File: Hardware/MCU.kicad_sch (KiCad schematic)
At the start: 30 parts, among them IC1 SN74AHC1G32DBVR, J3 SWD, SW1 RST, SW2 BOOT, U5 STM32L431CBTx, Y1 8M

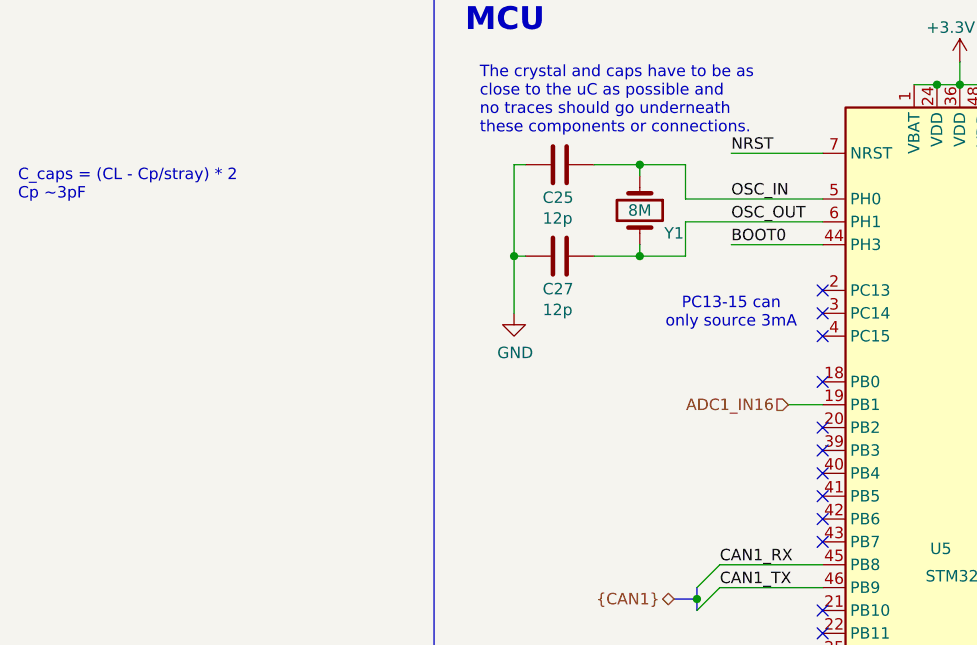
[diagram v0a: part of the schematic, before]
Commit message: differential amp for LPF
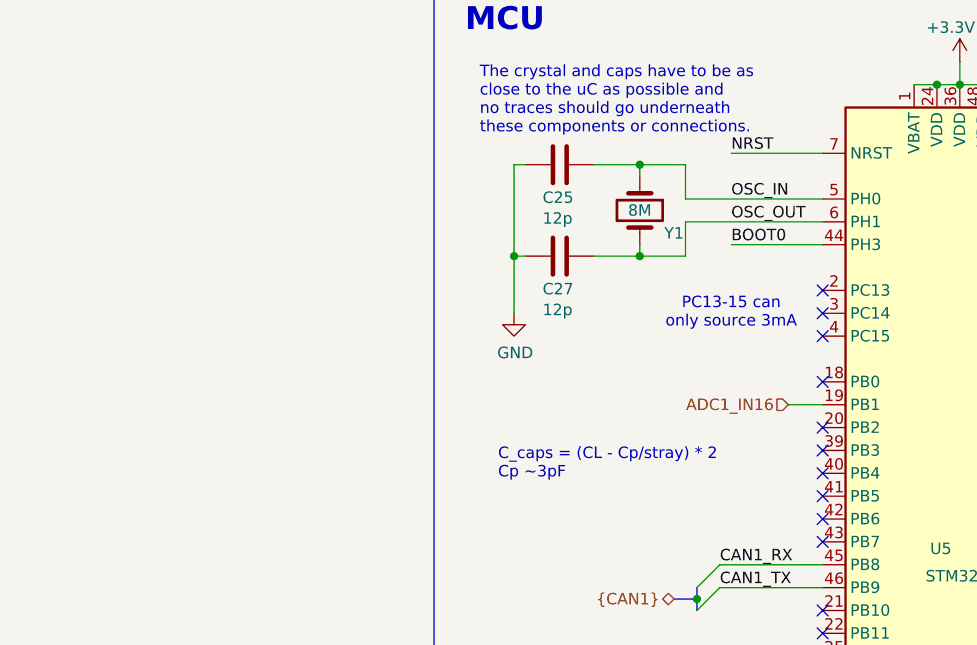
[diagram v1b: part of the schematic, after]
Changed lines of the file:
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@@
 	(text "C_caps = (CL - Cp/stray) * 2\nCp ~3pF"
 		(exclude_from_sim no)
-		(at -30.988 39.116 0)
+		(at 22.352 70.104 0)
 		(effects
 			(font

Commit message: diff amp / LPF
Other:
- note added: "Boot_GPIO is tied to PA7"
- note removed: "TODO: tie Boot_GPIO to a pin"
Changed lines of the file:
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@@
 		)
 	)
-	(text "TODO: tie Boot_GPIO to a pin"
+	(text "Boot_GPIO is tied to PA7"
 		(exclude_from_sim no)
 		(at 152.654 147.32 0)

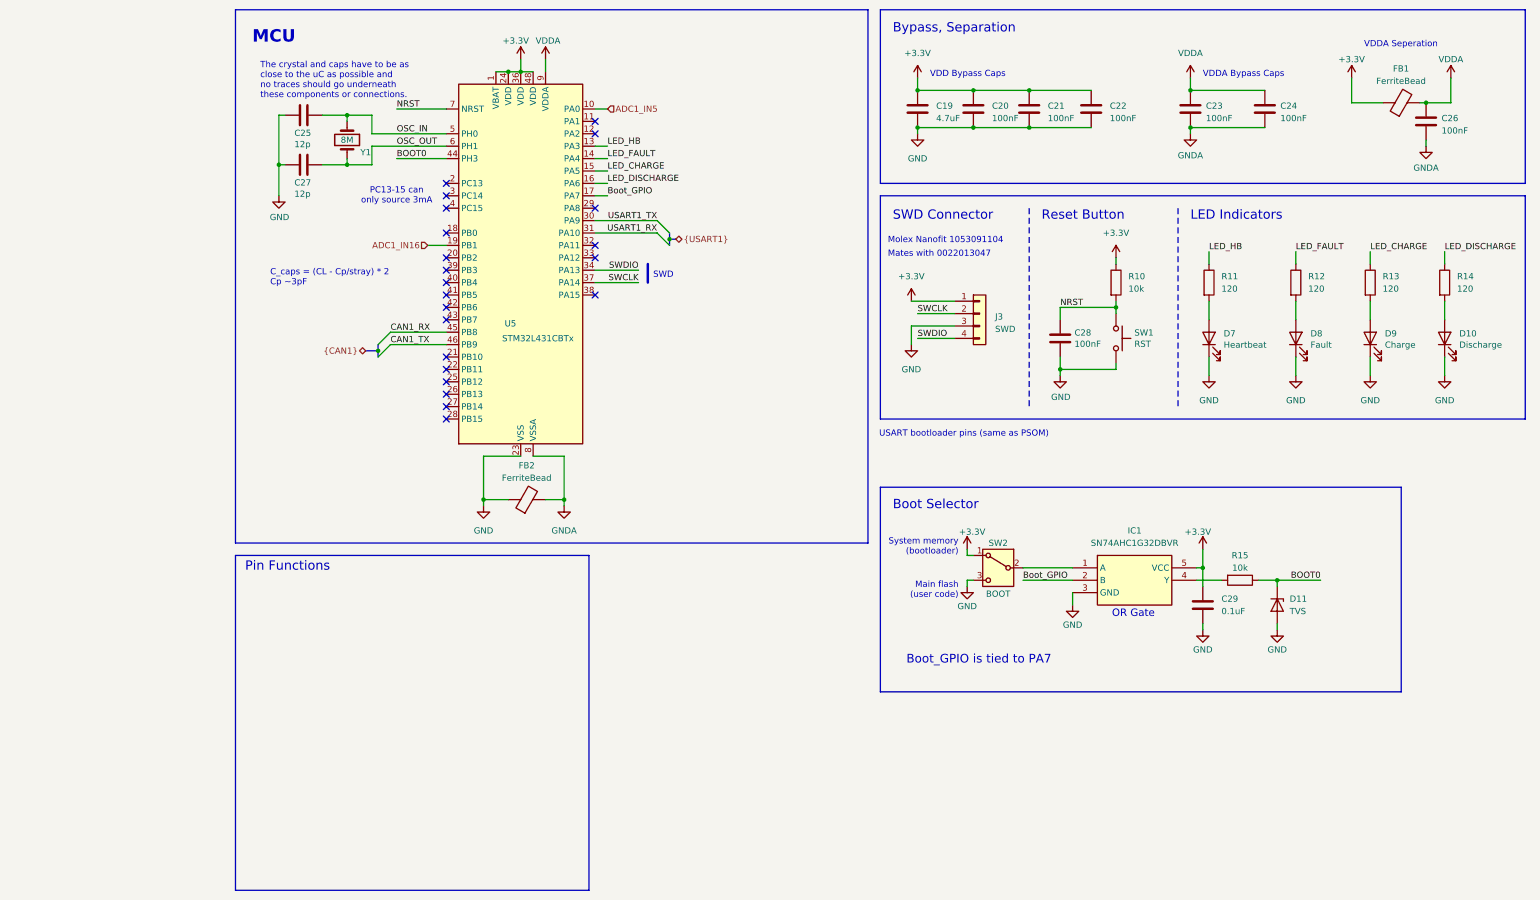
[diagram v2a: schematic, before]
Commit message: refactored and added LPF docs; added fuse, boot_gpio from USB-UART chip
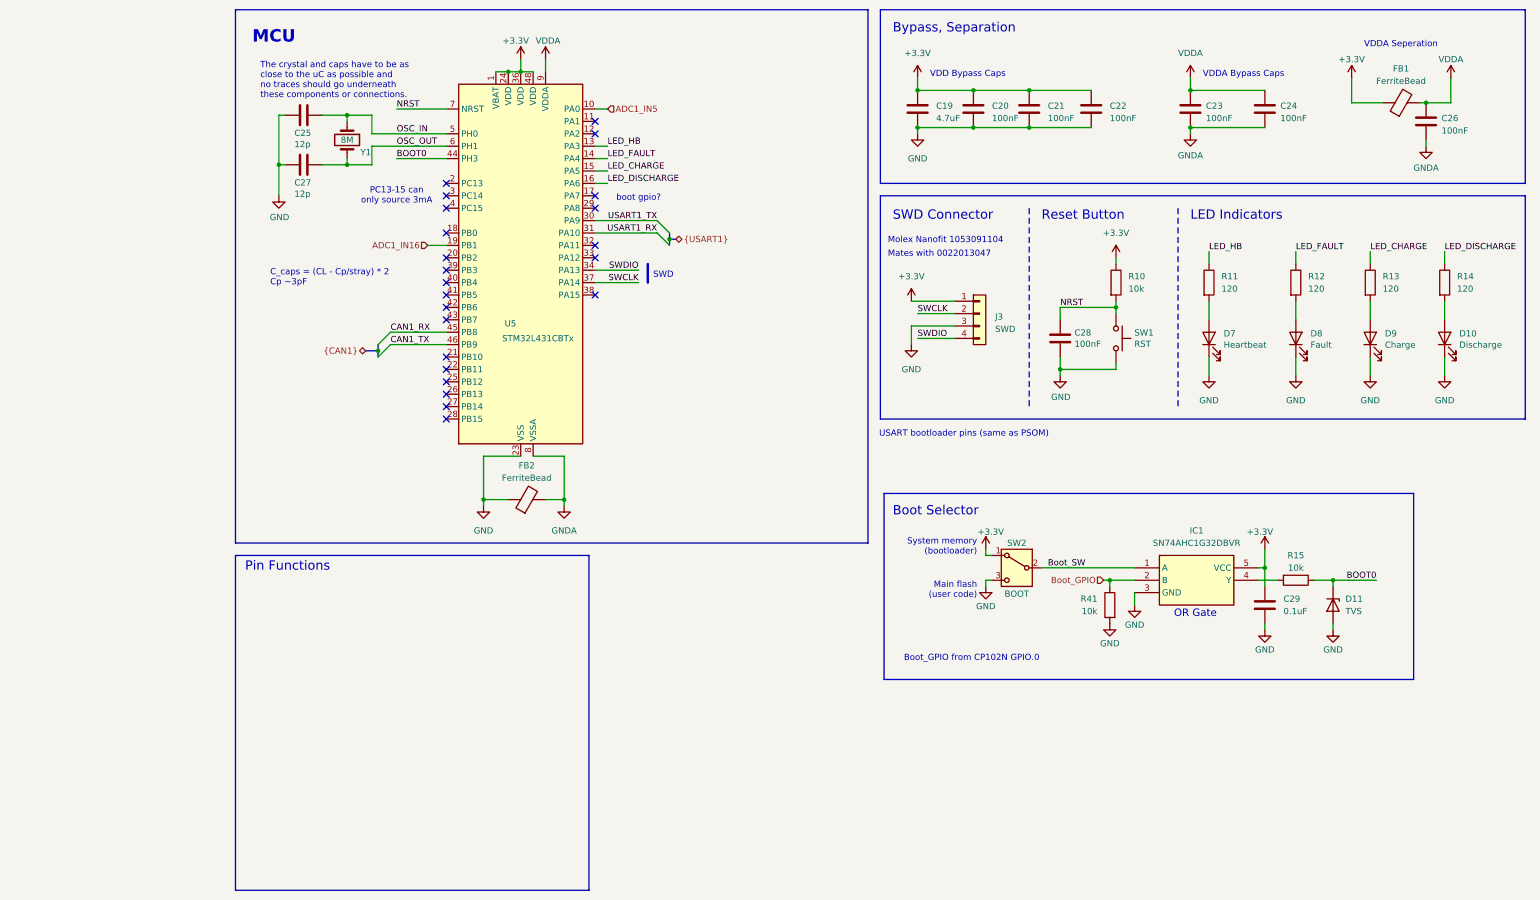
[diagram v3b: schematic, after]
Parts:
- added R41: 10k, symbol Device:R
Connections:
- net Boot_GPIO: now also R41.1; no longer U5.17 (PA7)
- net GND: now also R41.2
- net Boot_SW: now reaches IC1.1 (A), SW2.2 (B)
- no-connect marks 22 -> 23
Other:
- note added: "Boot_GPIO from CP102N GPIO.0"
- note added: "boot gpio?"
- note removed: "Boot_GPIO is tied to PA7"
- moved on the sheet: C29, D11, IC1, R15, SW2

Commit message: slightly cooked
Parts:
- R41: footprint (none) -> Resistor_SMD:R_0603_1608Metric_Pad0.98x0.95mm_HandSolder
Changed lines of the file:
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@@
 			)
 		)
-		(property "Footprint" ""
+		(property "Footprint" "Resistor_SMD:R_0603_1608Metric_Pad0.98x0.95mm_HandSolder"
 			(at 196.088 137.16 90)
 			(effects

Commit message: started layout not really but kind of
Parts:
- removed R41: 10k, Resistor_SMD:R_0603_1608Metric_Pad0.98x0.95mm_HandSolder, symbol Device:R
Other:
- moved on the sheet: C29, D11, IC1, R15

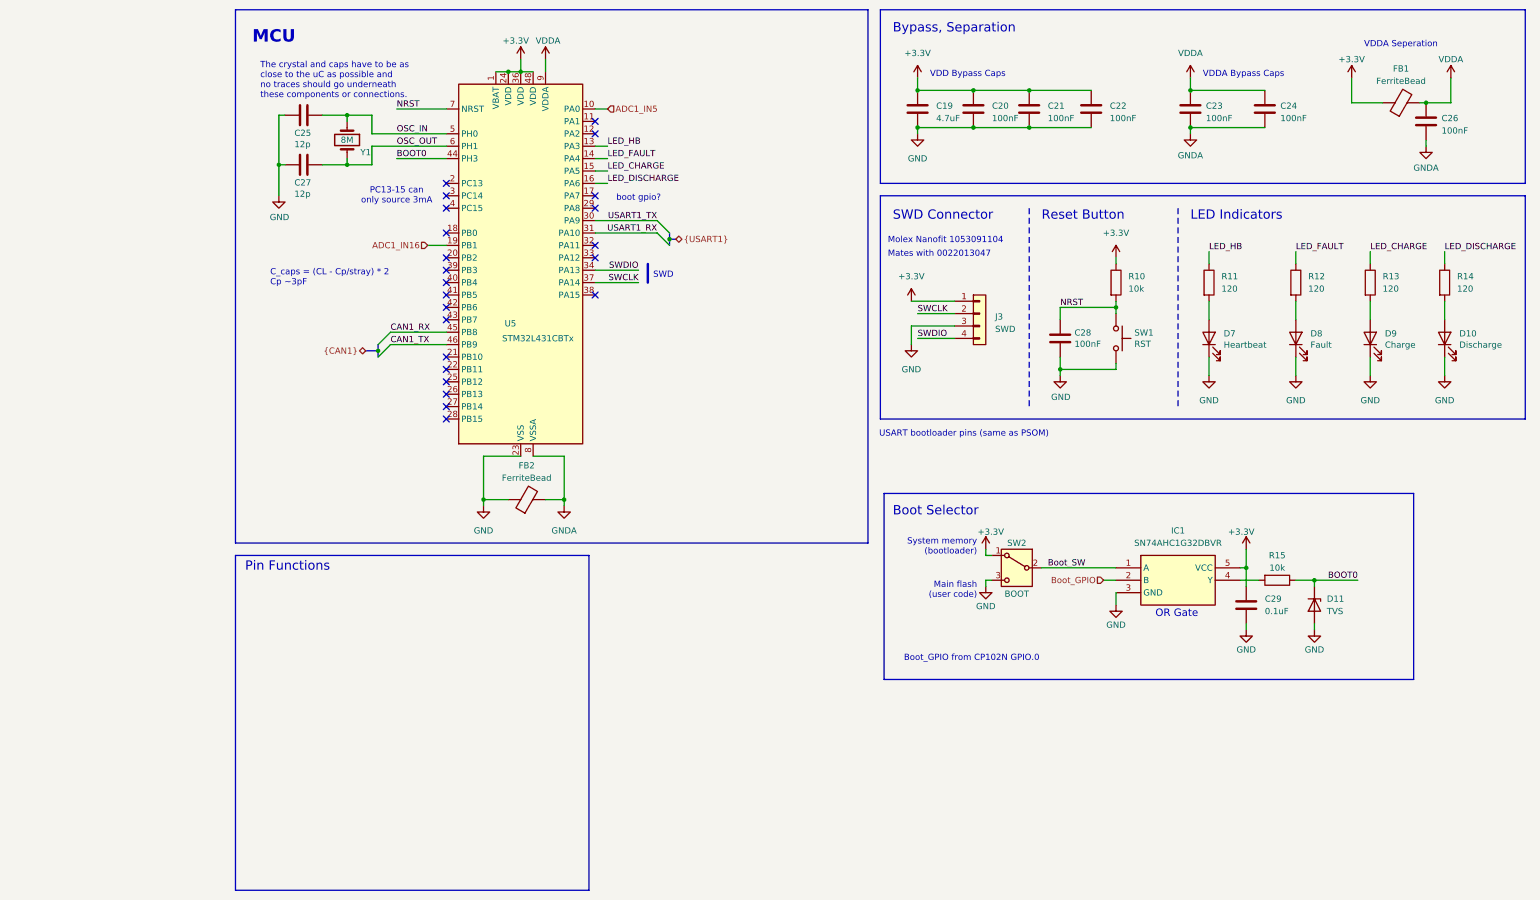
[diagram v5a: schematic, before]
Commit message: post review council sch changes: shielded connectors, removed SHDN resistor, diode OR for boot, standardized resistors
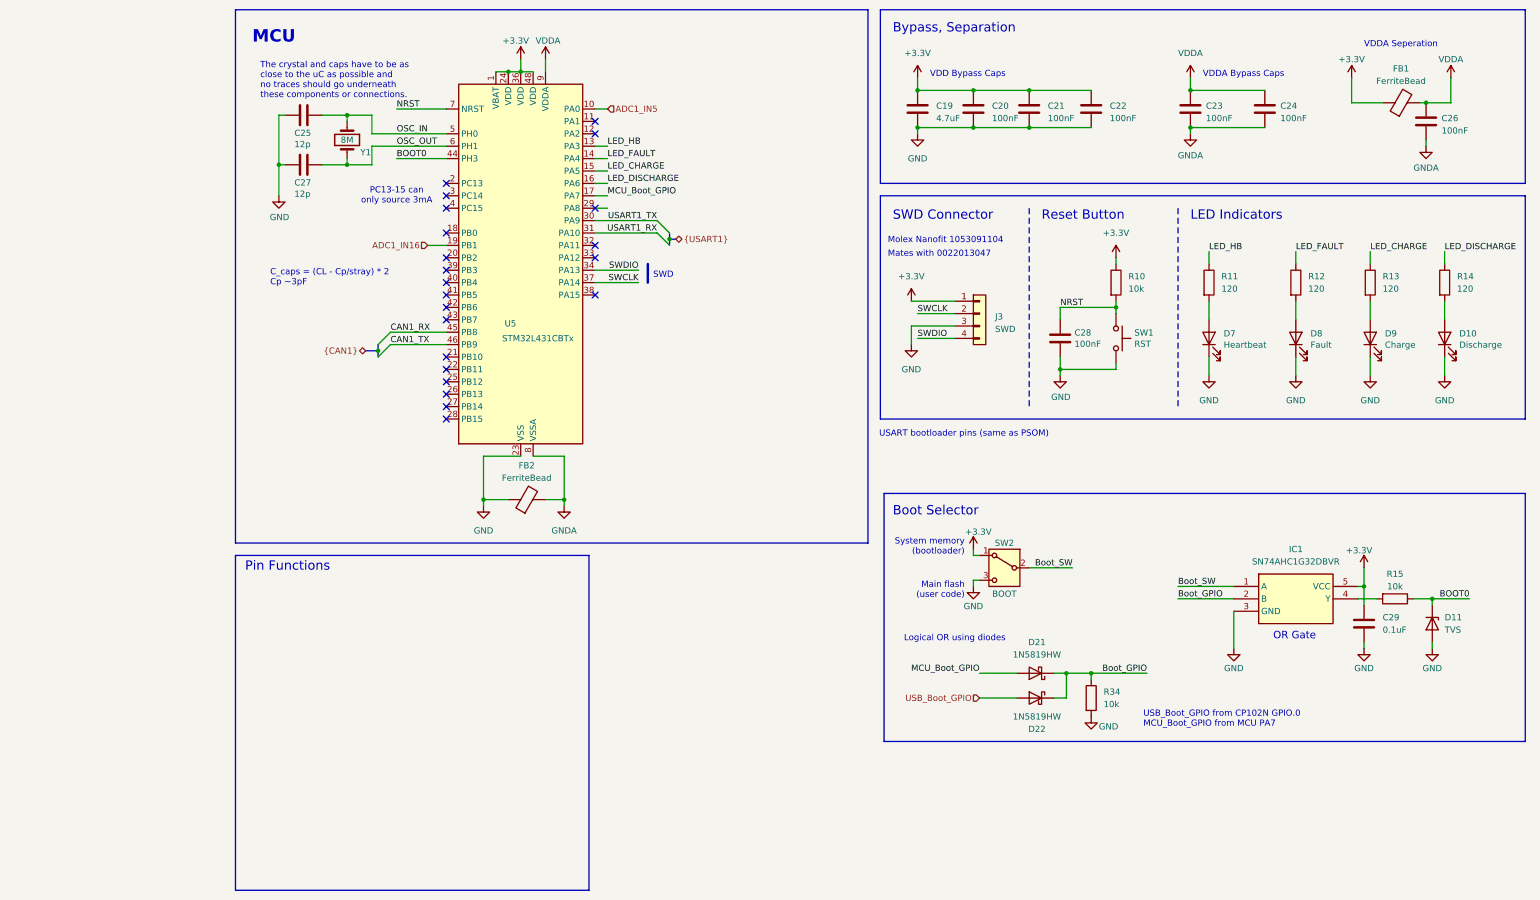
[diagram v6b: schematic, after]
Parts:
- added D21, D22: 1N5819HW, Diode_SMD:D_SOD-123, symbol Device:D_Schottky
- added R34: 10k, symbol Device:R
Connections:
- net Boot_GPIO: now also D21.1 (K), D22.1 (K), R34.1
- net GND: now also R34.2
- net MCU_Boot_GPIO: now reaches U5.17 (PA7)
- net MCU_Boot_GPIO: now also D21.2 (A)
- new net USB_Boot_GPIO: D22.2 (A)
- no-connect marks 23 -> 22
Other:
- note added: "Logical OR using diodes"
- note added: "USB_Boot_GPIO from CP102N GPIO.0 MCU_Boot_GPIO from MCU PA7"
- note removed: "Boot_GPIO from CP102N GPIO.0"
- note removed: "boot gpio?"
- moved on the sheet: C29, D11, IC1, R15, SW2

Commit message: starting routing i think
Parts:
- R34: footprint (none) -> Resistor_SMD:R_0603_1608Metric_Pad0.98x0.95mm_HandSolder
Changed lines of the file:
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@@
 			)
 		)
-		(property "Footprint" ""
+		(property "Footprint" "Resistor_SMD:R_0603_1608Metric_Pad0.98x0.95mm_HandSolder"
 			(at 188.722 156.21 90)
 			(effects
